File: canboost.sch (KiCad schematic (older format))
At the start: 12 parts, among them IC1 MCP2551-I/SN, P1 CONN_10X2, P2 CONN_10X2, P3 CONN_2

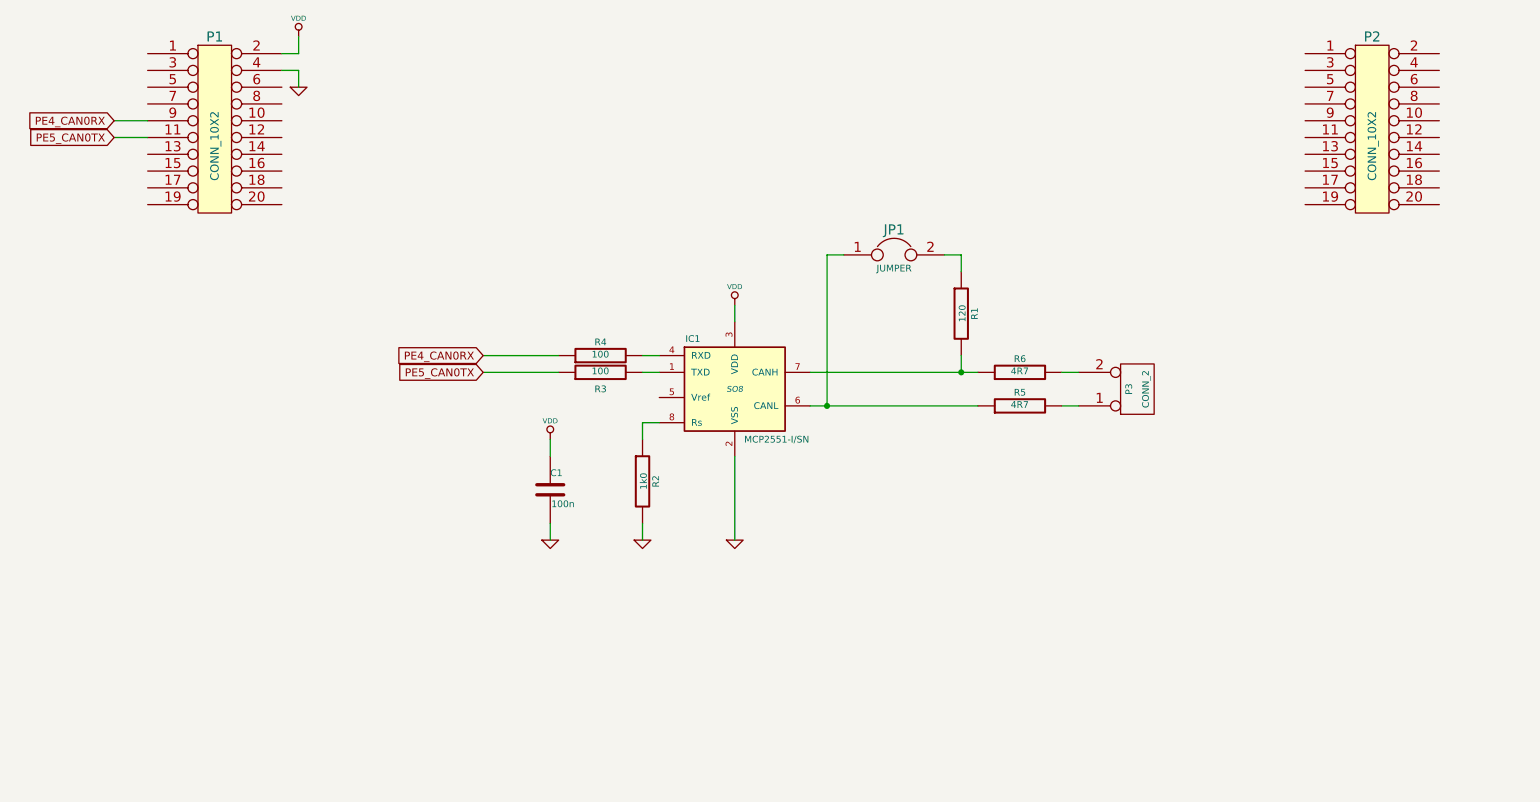
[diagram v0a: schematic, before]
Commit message: schematic seems to be finished
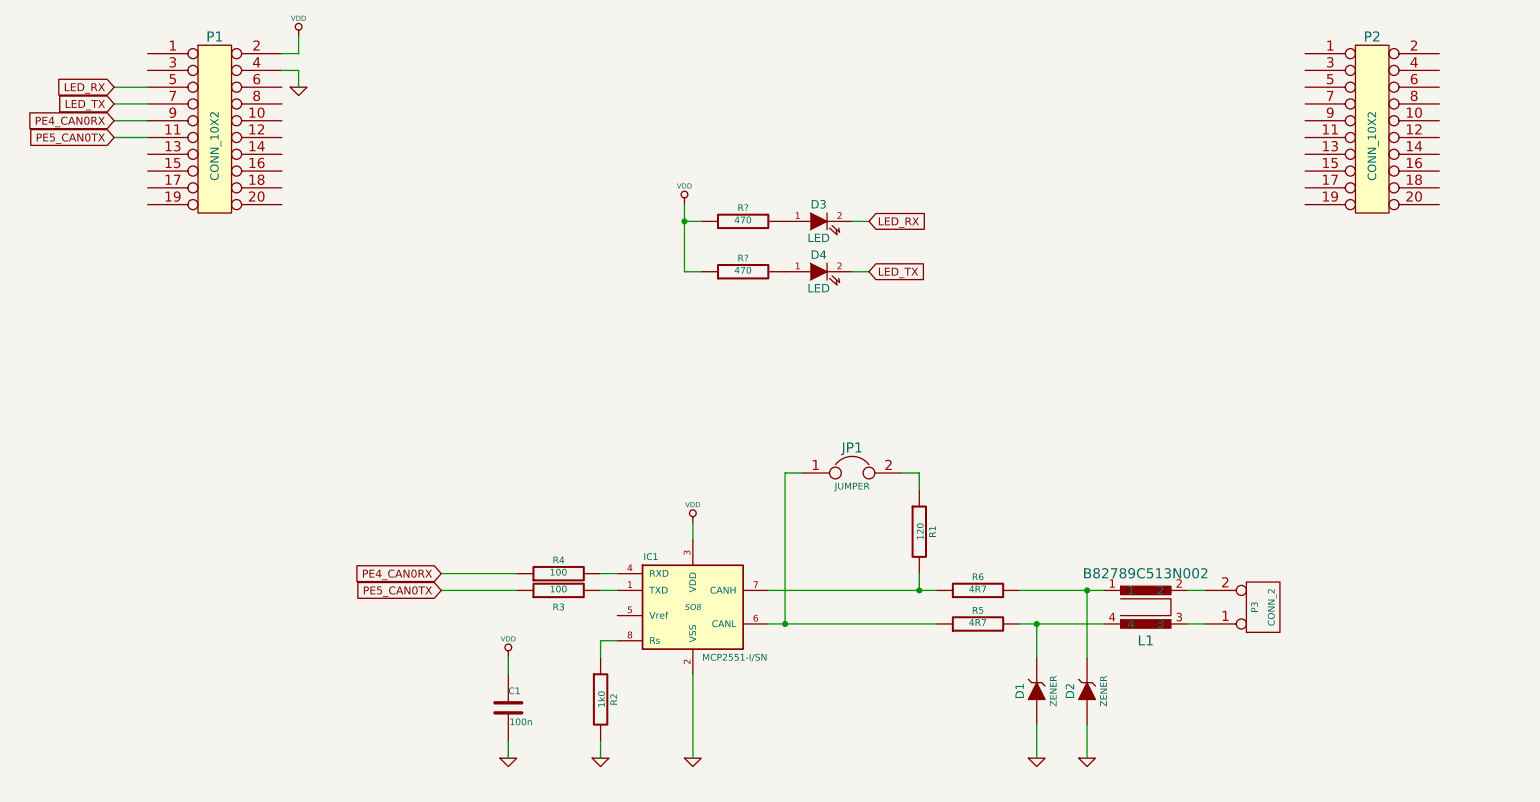
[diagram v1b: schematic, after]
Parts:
- added D1, D2: ZENER, ~, symbol ZENER
- added D3, D4: LED, ~, symbol LED
- added L1: B82789C513N002, ~, symbol BUS_CHOKE
- added R? (x2): 470, ~, symbol R
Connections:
- net GND: now also D1.1 (A), D2.1 (A)
- net VDD: now also R?.1, R?.1
- net at P3.1 (P1): now also L1.3; no longer R5.2
- net at P3.2 (PM): now also L1.2; no longer R6.2
- net LED_RX: now reaches P1.5 (P5)
- net LED_RX: now also D3.2 (K)
- net LED_TX: now reaches P1.7 (P7)
- net LED_TX: now also D4.2 (K)
- new net: D2.2 (K), L1.1, R6.2
- new net: D1.2 (K), L1.4, R5.2
- new net: D3.1 (A), R?.2
- new net: D4.1 (A), R?.2
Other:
- moved on the sheet: C1, IC1, JP1, P3, R1, R2, R3, R4, R5, R6

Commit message: netlist, footprint assigned
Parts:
- C1, R1, R2, R3, R4, R5, R6: footprint ~ -> SMD_Packages:SMD-0805
- D1, D2: footprint ~ -> Diodes_SMD:Diode-SMA_Handsoldering
- D3, D4: footprint ~ -> LEDs:LED-0805
- IC1: footprint SO8 -> Housings_SOIC:SOIC-8_3.9x4.9mm_Pitch1.27mm
- JP1: footprint ~ -> Pin_Headers:Pin_Header_Straight_1x02
- L1: footprint ~ -> My footprints:SIMDAD_1812
- P1, P2: footprint (none) -> Pin_Headers:Pin_Header_Straight_2x10
- P3: footprint (none) -> Sockets_MOLEX_KK-System:Socket_MOLEX-KK-RM3-96mm_Lock_2pin_straight
- R7, R8: renamed from R?; footprint ~ -> SMD_Packages:SMD-0805
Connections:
- net LED_RX renamed PB0_LED_RX
- net LED_TX renamed PB1_LED_TX
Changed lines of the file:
@@
 LIBS:bus_choke
 LIBS:canboost-cache
-EELAYER 27 0
+EELAYER 25 0
 EELAYER END
 $Descr A4 11693 8268
@@
 F 0 "IC1" H 5100 5400 40  0000 C CNN
 F 1 "MCP2551-I/SN" H 5600 4800 40  0000 C CNN
-F 2 "SO8" H 5350 5100 35  0000 C CIN
+F 2 "Housings_SOIC:SOIC-8_3.9x4.9mm_Pitch1.27mm" H 6000 4700 30  0000 C CIN
 F 3 "" H 5350 5100 60  0000 C CNN
 	1    5350 5100
@@
 F 0 "P3" V 8700 5100 40  0000 C CNN
 F 1 "CONN_2" V 8800 5100 40  0000 C CNN
-F 2 "" H 8750 5100 60  0000 C CNN
+F 2 "Sockets_MOLEX_KK-System:Socket_MOLEX-KK-RM3-96mm_Lock_2pin_straight" H 8750 5400 30  0000 C CNN
 F 3 "" H 8750 5100 60  0000 C CNN
 	1    8750 5100
@@
 $EndComp
 Wire Wire Line
-	5800 5000 6800 5000
-Wire Wire Line
-	5800 5200 6800 5200
+	5800 5000 6700 5000
+Wire Wire Line
+	6700 5000 6800 5000
+Wire Wire Line
+	5800 5200 5900 5200
+Wire Wire Line
+	5900 5200 6800 5200
 $Comp
 L R R1
@@
 F 0 "R1" V 6780 4650 40  0000 C CNN
 F 1 "120" V 6707 4651 40  0000 C CNN
-F 2 "~" V 6630 4650 30  0000 C CNN
+F 2 "SMD_Packages:SMD-0805" H 7100 4550 30  0000 C CNN
 F 3 "~" H 6700 4650 30  0000 C CNN
 	1    6700 4650
@@
 F 0 "JP1" H 6300 4450 60  0000 C CNN
 F 1 "JUMPER" H 6300 4220 40  0000 C CNN
-F 2 "~" H 6300 4300 60  0000 C CNN
+F 2 "Pin_Headers:Pin_Header_Straight_1x02" H 6300 4550 30  0000 C CNN
 F 3 "~" H 6300 4300 60  0000 C CNN
 	1    6300 4300
@@
 	5900 4300 5900 5200
 $Comp
-L GND #PWR?
+L GND #PWR01
 U 1 1 546E42D4
 P 5350 6000
-F 0 "#PWR?" H 5350 6000 30  0001 C CNN
+F 0 "#PWR01" H 5350 6000 30  0001 C CNN
 F 1 "GND" H 5350 5930 30  0001 C CNN
 F 2 "" H 5350 6000 60  0000 C CNN
@@
 	5350 5500 5350 6000
 $Comp
-L VDD #PWR?
+L VDD #PWR02
 U 1 1 546E42FC
 P 5350 4600
-F 0 "#PWR?" H 5350 4700 30  0001 C CNN
+F 0 "#PWR02" H 5350 4700 30  0001 C CNN
 F 1 "VDD" H 5350 4710 30  0000 C CNN
 F 2 "" H 5350 4600 60  0000 C CNN
@@
 F 0 "R2" V 4880 5650 40  0000 C CNN
 F 1 "1k0" V 4807 5651 40  0000 C CNN
-F 2 "~" V 4730 5650 30  0000 C CNN
+F 2 "SMD_Packages:SMD-0805" V 4700 5650 30  0000 C CNN
 F 3 "~" H 4800 5650 30  0000 C CNN
 	1    4800 5650
@@
 	4800 5300 4900 5300
 $Comp
-L GND #PWR?
+L GND #PWR03
 U 1 1 546E436D
 P 4800 6000
-F 0 "#PWR?" H 4800 6000 30  0001 C CNN
+F 0 "#PWR03" H 4800 6000 30  0001 C CNN
 F 1 "GND" H 4800 5930 30  0001 C CNN
 F 2 "" H 4800 6000 60  0000 C CNN
@@
 F 0 "R4" V 4630 4900 40  0000 C CNN
 F 1 "100" V 4557 4901 40  0000 C CNN
-F 2 "~" V 4480 4900 30  0000 C CNN
+F 2 "SMD_Packages:SMD-0805" V 4700 4900 30  0000 C CNN
 F 3 "~" H 4550 4900 30  0000 C CNN
 	1    4550 4900
@@
 F 0 "R3" V 4450 5000 40  0000 C CNN
 F 1 "100" V 4557 5001 40  0000 C CNN
-F 2 "~" V 4480 5000 30  0000 C CNN
+F 2 "SMD_Packages:SMD-0805" V 4400 5000 30  0000 C CNN
 F 3 "~" H 4550 5000 30  0000 C CNN
 	1    4550 5000
@@
 	4300 5000 3850 5000
 $Comp
-L GND #PWR?
+L GND #PWR04
 U 1 1 546E45DE
 P 4250 6000
-F 0 "#PWR?" H 4250 6000 30  0001 C CNN
+F 0 "#PWR04" H 4250 6000 30  0001 C CNN
 F 1 "GND" H 4250 5930 30  0001 C CNN
 F 2 "" H 4250 6000 60  0000 C CNN
@@
 F 0 "C1" H 4250 5800 40  0000 L CNN
 F 1 "100n" H 4256 5615 40  0000 L CNN
-F 2 "~" H 4288 5550 30  0000 C CNN
+F 2 "SMD_Packages:SMD-0805" V 4100 5750 30  0000 C CNN
 F 3 "~" H 4250 5700 60  0000 C CNN
 	1    4250 5700
@@
 $EndComp
 $Comp
-L VDD #PWR?
+L VDD #PWR05
 U 1 1 546E4613
 P 4250 5400
-F 0 "#PWR?" H 4250 5500 30  0001 C CNN
+F 0 "#PWR05" H 4250 5500 30  0001 C CNN
 F 1 "VDD" H 4250 5510 30  0000 C CNN
 F 2 "" H 4250 5400 60  0000 C CNN
@@
 F 0 "P1" H 2500 2800 60  0000 C CNN
 F 1 "CONN_10X2" V 2500 2150 50  0000 C CNN
-F 2 "" H 2500 2250 60  0000 C CNN
+F 2 "Pin_Headers:Pin_Header_Straight_2x10" H 2500 1650 30  0000 C CNN
 F 3 "" H 2500 2250 60  0000 C CNN
 	1    2500 2250
@@
 F 0 "P2" H 9400 2800 60  0000 C CNN
 F 1 "CONN_10X2" V 9400 2150 50  0000 C CNN
-F 2 "" H 9400 2250 60  0000 C CNN
+F 2 "Pin_Headers:Pin_Header_Straight_2x10" H 9400 1650 30  0000 C CNN
 F 3 "" H 9400 2250 60  0000 C CNN
 	1    9400 2250
@@
 $EndComp
 $Comp
-L GND #PWR?
+L GND #PWR06
 U 1 1 546E4CA4
 P 3000 2000
-F 0 "#PWR?" H 3000 2000 30  0001 C CNN
+F 0 "#PWR06" H 3000 2000 30  0001 C CNN
 F 1 "GND" H 3000 1930 30  0001 C CNN
 F 2 "" H 3000 2000 60  0000 C CNN
@@
 $EndComp
 $Comp
-L VDD #PWR?
+L VDD #PWR07
 U 1 1 546E4CAF
 P 3000 1700
-F 0 "#PWR?" H 3000 1800 30  0001 C CNN
+F 0 "#PWR07" H 3000 1800 30  0001 C CNN
 F 1 "VDD" H 3000 1810 30  0000 C CNN
 F 2 "" H 3000 1700 60  0000 C CNN
@@
 F 0 "R6" V 7130 5000 40  0000 C CNN
 F 1 "4R7" V 7057 5001 40  0000 C CNN
-F 2 "~" V 6980 5000 30  0000 C CNN
+F 2 "SMD_Packages:SMD-0805" V 7200 4900 30  0000 C CNN
 F 3 "~" H 7050 5000 30  0000 C CNN
 	1    7050 5000
@@
 $EndComp
 Wire Wire Line
-	7300 5000 7800 5000
+	7300 5000 7700 5000
+Wire Wire Line
+	7700 5000 7800 5000
 $Comp
 L R R5
@@
 F 0 "R5" V 7130 5200 40  0000 C CNN
 F 1 "4R7" V 7057 5201 40  0000 C CNN
-F 2 "~" V 6980 5200 30  0000 C CNN
+F 2 "SMD_Packages:SMD-0805" V 6950 5200 30  0000 C CNN
 F 3 "~" H 7050 5200 30  0000 C CNN
 	1    7050 5200
@@
 $EndComp
 Wire Wire Line
-	7300 5200 7800 5200
+	7300 5200 7400 5200
+Wire Wire Line
+	7400 5200 7800 5200
 $Comp
 L ZENER D1
@@
 F 0 "D1" H 7400 5700 50  0000 C CNN
 F 1 "ZENER" H 7400 5500 40  0000 C CNN
-F 2 "~" H 7400 5600 60  0000 C CNN
+F 2 "Diodes_SMD:Diode-SMA_Handsoldering" V 6900 5400 30  0000 C CNN
 F 3 "~" H 7400 5600 60  0000 C CNN
 	1    7400 5600
@@
 F 0 "D2" H 7700 5700 50  0000 C CNN
 F 1 "ZENER" H 7700 5500 40  0000 C CNN
-F 2 "~" H 7700 5600 60  0000 C CNN
+F 2 "Diodes_SMD:Diode-SMA_Handsoldering" V 7150 5700 30  0000 C CNN
 F 3 "~" H 7700 5600 60  0000 C CNN
 	1    7700 5600
@@
 Connection ~ 7700 5000
 $Comp
-L GND #PWR?
+L GND #PWR08
 U 1 1 546F8269
 P 7400 6000
-F 0 "#PWR?" H 7400 6000 30  0001 C CNN
+F 0 "#PWR08" H 7400 6000 30  0001 C CNN
 F 1 "GND" H 7400 5930 30  0001 C CNN
 F 2 "" H 7400 6000 60  0000 C CNN
@@
 $EndComp
 $Comp
-L GND #PWR?
+L GND #PWR09
 U 1 1 546F826F
 P 7700 6000
-F 0 "#PWR?" H 7700 6000 30  0001 C CNN
+F 0 "#PWR09" H 7700 6000 30  0001 C CNN
 F 1 "GND" H 7700 5930 30  0001 C CNN
 F 2 "" H 7700 6000 60  0000 C CNN
@@
 F 0 "D3" H 6100 2900 50  0000 C CNN
 F 1 "LED" H 6100 2700 50  0000 C CNN
-F 2 "~" H 6100 2800 60  0000 C CNN
+F 2 "LEDs:LED-0805" H 6100 3000 30  0000 C CNN
 F 3 "~" H 6100 2800 60  0000 C CNN
 	1    6100 2800
@@
 F 0 "D4" H 6100 3200 50  0000 C CNN
 F 1 "LED" H 6100 3000 50  0000 C CNN
-F 2 "~" H 6100 3100 60  0000 C CNN
+F 2 "LEDs:LED-0805" H 6100 2900 30  0000 C CNN
 F 3 "~" H 6100 3100 60  0000 C CNN
 	1    6100 3100
@@
 $EndComp
 $Comp
-L R R?
+L R R7
 U 1 1 546F8416
 P 5650 2800
-F 0 "R?" V 5730 2800 40  0000 C CNN
+F 0 "R7" V 5730 2800 40  0000 C CNN
 F 1 "470" V 5657 2801 40  0000 C CNN
-F 2 "~" V 5580 2800 30  0000 C CNN
+F 2 "SMD_Packages:SMD-0805" V 5550 2800 30  0000 C CNN
 F 3 "~" H 5650 2800 30  0000 C CNN
 	1    5650 2800
@@
 $EndComp
 $Comp
-L R R?
+L R R8
 U 1 1 546F8425
 P 5650 3100
-F 0 "R?" V 5730 3100 40  0000 C CNN
+F 0 "R8" V 5730 3100 40  0000 C CNN
 F 1 "470" V 5657 3101 40  0000 C CNN
-F 2 "~" V 5580 3100 30  0000 C CNN
+F 2 "SMD_Packages:SMD-0805" V 5800 3100 30  0000 C CNN
 F 3 "~" H 5650 3100 30  0000 C CNN
 	1    5650 3100
@@
 $EndComp
 $Comp
-L VDD #PWR?
+L VDD #PWR010
 U 1 1 546F8486
 P 5300 2700
-F 0 "#PWR?" H 5300 2800 30  0001 C CNN
+F 0 "#PWR010" H 5300 2800 30  0001 C CNN
 F 1 "VDD" H 5300 2810 30  0000 C CNN
 F 2 "" H 5300 2700 60  0000 C CNN
@@
 $EndComp
 Wire Wire Line
-	5300 2700 5300 3100
+	5300 2700 5300 2800
+Wire Wire Line
+	5300 2800 5300 3100
 Wire Wire Line
 	5300 3100 5400 3100
@@
 	6300 2800 6400 2800
 Text GLabel 6400 2800 2    47   Input ~ 0
-LED_RX
+PB0_LED_RX
 Text GLabel 6400 3100 2    47   Input ~ 0
-LED_TX
+PB1_LED_TX
 $Comp
 L BUS_CHOKE L1
@@
 F 0 "L1" H 8050 4900 60  0000 C CNN
 F 1 "B82789C513N002" H 8050 5300 60  0000 C CNN
-F 2 "~" H 8050 5100 60  0000 C CNN
+F 2 "My footprints:SIMDAD_1812" H 8050 5400 30  0000 C CNN
 F 3 "~" H 8050 5100 60  0000 C CNN
 	1    8050 5100
@@
 	8300 5200 8400 5200
 Text GLabel 1900 2000 0    47   Input ~ 0
-LED_RX
+PB0_LED_RX
 Text GLabel 1900 2100 0    47   Input ~ 0
-LED_TX
+PB1_LED_TX
 Wire Wire Line
 	1900 2000 2100 2000

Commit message: layout complete (v0.10)
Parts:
- R1, R5, R6: footprint SMD_Packages:SMD-0805 -> SMD_Packages:SMD-1206
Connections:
- net GND: now also D3.2 (K), D4.2 (K), P2.2 (P2)
- net PB0_LED_RX: now also P2.15 (P15), R7.2; no longer D3.2 (K), P1.5 (P5)
- net PB1_LED_TX: now also P2.17 (P17), R8.2; no longer D4.2 (K), P1.7 (P7)
- net VDD: no longer R7.1, R8.1
- net at IC1.6 (CANL), R5.1: no longer JP1.1
- net at IC1.7 (CANH), R6.1: no longer R1.2
- net CANH: now reaches L1.3
- net CANH: now also P3.2 (PM), R1.2; no longer P3.1 (P1)
- net CANL: now reaches L1.2
- net CANL: now also JP1.1, P3.1 (P1); no longer P3.2 (PM)
- net at D2.2 (K), R6.2: now also L1.4; no longer L1.1
- net at D1.2 (K), R5.2: now also L1.1; no longer L1.4
- net at D3.1 (A): now also R7.1; no longer R7.2
- net at D4.1 (A): now also R8.1; no longer R8.2
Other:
- moved on the sheet: C1, D1, D2, D3, D4, IC1, JP1, L1, P3, R1, R2, R3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
